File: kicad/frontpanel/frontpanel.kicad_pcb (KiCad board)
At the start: 2 copper layers, 40.6 x 128.5 mm, 21 parts

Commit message: Update frontpanel.
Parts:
- moved REF** 0.64 mm to (120.4, 39.5)
- moved REF** 0.64 mm to (120.4, 56.3)
- moved REF** 0.63 mm to (133.1, 39.5)
- moved REF** 0.63 mm to (145.8, 56.3)
- moved REF** 0.63 mm to (133.1, 56.3)
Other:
- board text added: "ACT"
- board text added: "ARP LEN"
- board text added: "CC1"
- board text added: "CC2"
- board text added: "CV1"
- board text added: "CV2"
- board text added: "GATE1"
- board text added: "GATE2"
- board text added: "JLCJLCJLCJLC"
- board text added: "MIDI IN"
- board text added: "Miarph"
- board text added: "P1"
- board text added: "P2"
- board text added: "P3"
- board text added: "P4"
- board text added: "P5"
- board text added: "P6"
- board text added: "P7"
- board text added: "P8"
- board text added: "TOMARUS"
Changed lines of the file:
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@@
   (general
     (thickness 1.6)
-    (drawings 16)
+    (drawings 34)
     (tracks 0)
     (zones 0)
@@
     (32 B.Adhes user hide)
     (33 F.Adhes user hide)
-    (34 B.Paste user hide)
-    (35 F.Paste user hide)
+    (34 B.Paste user)
+    (35 F.Paste user)
     (36 B.SilkS user)
     (37 F.SilkS user)
@@
     (39 F.Mask user hide)
     (40 Dwgs.User user hide)
-    (41 Cmts.User user)
+    (41 Cmts.User user hide)
     (42 Eco1.User user)
     (43 Eco2.User user hide)
@@
   )
   (module MountingHole:MountingHole_6.4mm_M6 (layer F.Cu)
-    (at 132.461 39.497)
+    (at 133.096 39.497)
     (descr "Mounting Hole 6.4mm, no annular, M6")
     (tags "mounting hole 6.4mm no annular m6")
@@
   )
   (module MountingHole:MountingHole_3.2mm_M3 (layer F.Cu)
-    (at 119.761 39.497)
+    (at 120.396 39.497)
     (descr "Mounting Hole 3.2mm, no annular, M3")
     (tags "mounting hole 3.2mm no annular m3")
@@
   )
   (module MountingHole:MountingHole_6.4mm_M6_Pad (layer F.Cu)
-    (at 119.761 56.261)
-    (descr "Mounting Hole 6.4mm, M6")
-    (tags "mounting hole 6.4mm m6")
-    (attr virtual)
-    (fp_text reference REF** (at 0 -7.4) (layer F.SilkS) hide
-      (effects (font (size 1 1) (thickness 0.15)))
-    )
-    (fp_text value MountingHole_6.4mm_M6_Pad (at 0 7.4) (layer F.Fab)
-      (effects (font (size 1 1) (thickness 0.15)))
-    )
-    (fp_circle (center 0 0) (end 6.65 0) (layer F.CrtYd) (width 0.05))
-    (fp_circle (center 0 0) (end 6.4 0) (layer Cmts.User) (width 0.15))
-    (fp_text user %R (at 0.3 0) (layer F.Fab)
-      (effects (font (size 1 1) (thickness 0.15)))
-    )
-    (pad 1 thru_hole circle (at 0 0) (size 8.4 8.4) (drill 6.4) (layers *.Cu *.Mask))
-  )
-  (module MountingHole:MountingHole_6.4mm_M6_Pad (layer F.Cu)
-    (at 145.161 56.261)
-    (descr "Mounting Hole 6.4mm, M6")
-    (tags "mounting hole 6.4mm m6")
-    (attr virtual)
-    (fp_text reference REF** (at 0 -7.4) (layer F.SilkS) hide
-      (effects (font (size 1 1) (thickness 0.15)))
-    )
-    (fp_text value MountingHole_6.4mm_M6_Pad (at 0 7.4) (layer F.Fab)
-      (effects (font (size 1 1) (thickness 0.15)))
-    )
-    (fp_circle (center 0 0) (end 6.65 0) (layer F.CrtYd) (width 0.05))
-    (fp_circle (center 0 0) (end 6.4 0) (layer Cmts.User) (width 0.15))
-    (fp_text user %R (at 0.3 0) (layer F.Fab)
-      (effects (font (size 1 1) (thickness 0.15)))
-    )
-    (pad 1 thru_hole circle (at 0 0) (size 8.4 8.4) (drill 6.4) (layers *.Cu *.Mask))
-  )
-  (module MountingHole:MountingHole_6.4mm_M6_Pad (layer F.Cu)
-    (at 132.461 56.261)
+    (at 120.396 56.261)
+    (descr "Mounting Hole 6.4mm, M6")
+    (tags "mounting hole 6.4mm m6")
+    (attr virtual)
+    (fp_text reference REF** (at 0 -7.4) (layer F.SilkS) hide
+      (effects (font (size 1 1) (thickness 0.15)))
+    )
+    (fp_text value MountingHole_6.4mm_M6_Pad (at 0 7.4) (layer F.Fab)
+      (effects (font (size 1 1) (thickness 0.15)))
+    )
+    (fp_circle (center 0 0) (end 6.65 0) (layer F.CrtYd) (width 0.05))
+    (fp_circle (center 0 0) (end 6.4 0) (layer Cmts.User) (width 0.15))
+    (fp_text user %R (at 0.3 0) (layer F.Fab)
+      (effects (font (size 1 1) (thickness 0.15)))
+    )
+    (pad 1 thru_hole circle (at 0 0) (size 8.4 8.4) (drill 6.4) (layers *.Cu *.Mask))
+  )
+  (module MountingHole:MountingHole_6.4mm_M6_Pad (layer F.Cu)
+    (at 145.796 56.261)
+    (descr "Mounting Hole 6.4mm, M6")
+    (tags "mounting hole 6.4mm m6")
+    (attr virtual)
+    (fp_text reference REF** (at 0 -7.4) (layer F.SilkS) hide
+      (effects (font (size 1 1) (thickness 0.15)))
+    )
+    (fp_text value MountingHole_6.4mm_M6_Pad (at 0 7.4) (layer F.Fab)
+      (effects (font (size 1 1) (thickness 0.15)))
+    )
+    (fp_circle (center 0 0) (end 6.65 0) (layer F.CrtYd) (width 0.05))
+    (fp_circle (center 0 0) (end 6.4 0) (layer Cmts.User) (width 0.15))
+    (fp_text user %R (at 0.3 0) (layer F.Fab)
+      (effects (font (size 1 1) (thickness 0.15)))
+    )
+    (pad 1 thru_hole circle (at 0 0) (size 8.4 8.4) (drill 6.4) (layers *.Cu *.Mask))
+  )
+  (module MountingHole:MountingHole_6.4mm_M6_Pad (layer F.Cu)
+    (at 133.096 56.261)
     (descr "Mounting Hole 6.4mm, M6")
     (tags "mounting hole 6.4mm m6")
@@
     )
     (pad 1 thru_hole circle (at 0 0) (size 8.4 8.4) (drill 6.4) (layers *.Cu *.Mask))
+  )
+  (gr_text JLCJLCJLCJLC (at 133.096 132.08) (layer F.SilkS)
+    (effects (font (size 1.5 1.5) (thickness 0.3)))
+  )
+  (gr_text ACT (at 120.396 43.18) (layer B.SilkS)
+    (effects (font (size 1 1) (thickness 0.25)) (justify mirror))
+  )
+  (gr_text "ARP LEN" (at 133.096 45.72) (layer B.SilkS)
+    (effects (font (size 1.5 1.5) (thickness 0.3)) (justify mirror))
+  )
+  (gr_text TOMARUS (at 132.842 140.081) (layer B.SilkS)
+    (effects (font (size 2.5 2.5) (thickness 0.5)) (justify mirror))
+  )
+  (gr_text Miarph (at 132.842 17.526) (layer B.SilkS)
+    (effects (font (size 3 3) (thickness 0.5)) (justify mirror))
+  )
+  (gr_text GATE2 (at 120.396 109.22) (layer B.SilkS)
+    (effects (font (size 1.5 1.5) (thickness 0.3)) (justify mirror))
+  )
+  (gr_text CV2 (at 120.396 93.98) (layer B.SilkS)
+    (effects (font (size 1.5 1.5) (thickness 0.3)) (justify mirror))
+  )
+  (gr_text GATE1 (at 120.396 78.74) (layer B.SilkS)
+    (effects (font (size 1.5 1.5) (thickness 0.3)) (justify mirror))
+  )
+  (gr_text CV1 (at 120.396 63.5) (layer B.SilkS)
+    (effects (font (size 1.5 1.5) (thickness 0.3)) (justify mirror))
+  )
+  (gr_text P6 (at 133.096 93.98) (layer B.SilkS)
+    (effects (font (size 1.5 1.5) (thickness 0.3)) (justify mirror))
+  )
+  (gr_text P5 (at 145.796 93.98) (layer B.SilkS)
+    (effects (font (size 1.5 1.5) (thickness 0.3)) (justify mirror))
+  )
+  (gr_text P4 (at 133.096 78.74) (layer B.SilkS)
+    (effects (font (size 1.5 1.5) (thickness 0.3)) (justify mirror))
+  )
+  (gr_text P3 (at 145.796 78.74) (layer B.SilkS)
+    (effects (font (size 1.5 1.5) (thickness 0.3)) (justify mirror))
+  )
+  (gr_text P2 (at 133.096 63.5) (layer B.SilkS)
+    (effects (font (size 1.5 1.5) (thickness 0.3)) (justify mirror))
+  )
+  (gr_text P1 (at 145.796 63.5) (layer B.SilkS)
+    (effects (font (size 1.5 1.5) (thickness 0.3)) (justify mirror))
+  )
+  (gr_text P8 (at 133.096 109.22) (layer B.SilkS)
+    (effects (font (size 1.5 1.5) (thickness 0.3)) (justify mirror))
+  )
+  (gr_text P7 (at 145.796 109.22) (layer B.SilkS)
+    (effects (font (size 1.5 1.5) (thickness 0.3)) (justify mirror))
+  )
+  (gr_text CC2 (at 120.396 124.46) (layer B.SilkS)
+    (effects (font (size 1.5 1.5) (thickness 0.3)) (justify mirror))
+  )
+  (gr_text CC1 (at 133.096 124.46) (layer B.SilkS)
+    (effects (font (size 1.5 1.5) (thickness 0.3)) (justify mirror))
+  )
+  (gr_text "MIDI IN" (at 145.796 124.46) (layer B.SilkS)
+    (effects (font (size 1.5 1.5) (thickness 0.3)) (justify mirror))
   )
   (dimension 40.607945 (width 0.3) (layer F.SilkS)
@@
   (gr_line (start 153.416 14.478) (end 153.416 14.732) (layer Edge.Cuts) (width 0.15))
   (dimension 128.491945 (width 0.3) (layer F.SilkS)
-    (gr_text "128.492 mm" (at 158.269779 78.755981 270.0006131) (layer F.SilkS)
+    (gr_text "128.492 mm" (at 158.904779 78.755981 270.0006131) (layer F.SilkS)
       (effects (font (size 1.5 1.5) (thickness 0.3)))
     )
-    (feature1 (pts (xy 153.884467 143.002) (xy 156.756888 143.001969)))
-    (feature2 (pts (xy 153.883092 14.510055) (xy 156.755513 14.510024)))
-    (crossbar (pts (xy 156.169092 14.510031) (xy 156.170467 143.001976)))
-    (arrow1a (pts (xy 156.170467 143.001976) (xy 155.584034 141.875479)))
-    (arrow1b (pts (xy 156.170467 143.001976) (xy 156.756876 141.875466)))
-    (arrow2a (pts (xy 156.169092 14.510031) (xy 155.582683 15.636541)))
-    (arrow2b (pts (xy 156.169092 14.510031) (xy 156.755525 15.636528)))
+    (feature1 (pts (xy 154.519467 143.002) (xy 157.391888 143.001969)))
+    (feature2 (pts (xy 154.518092 14.510055) (xy 157.390513 14.510024)))
+    (crossbar (pts (xy 156.804092 14.510031) (xy 156.805467 143.001976)))
+    (arrow1a (pts (xy 156.805467 143.001976) (xy 156.219034 141.875479)))
+    (arrow1b (pts (xy 156.805467 143.001976) (xy 157.391876 141.875466)))
+    (arrow2a (pts (xy 156.804092 14.510031) (xy 156.217683 15.636541)))
+    (arrow2b (pts (xy 156.804092 14.510031) (xy 157.390525 15.636528)))
   )
   (gr_line (start 153.416 142.748) (end 153.416 127) (layer Edge.Cuts) (width 0.15))
@@
   (gr_line (start 112.776 30.48) (end 112.776 14.732) (layer Edge.Cuts) (width 0.15))
   (gr_line (start 112.776 127) (end 112.776 30.48) (layer Edge.Cuts) (width 0.15))
-  (gr_line (start 153.416 127) (end 112.776 127) (layer Edge.Cuts) (width 0.15))
   (gr_line (start 153.416 30.48) (end 153.416 127) (layer Edge.Cuts) (width 0.15))
-  (gr_line (start 112.776 30.48) (end 153.416 30.48) (layer Edge.Cuts) (width 0.15))
 )

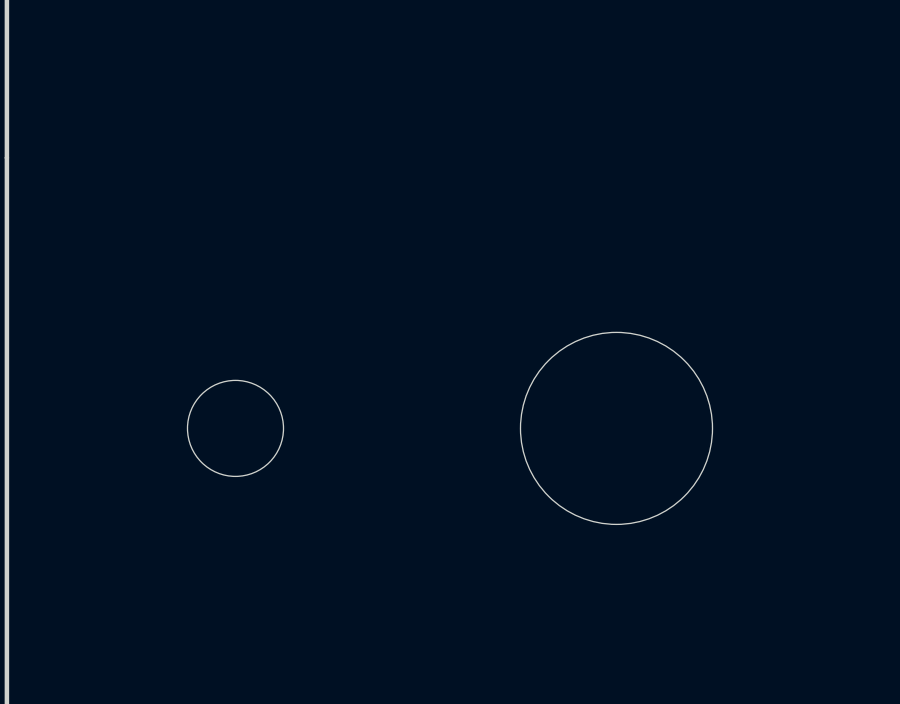
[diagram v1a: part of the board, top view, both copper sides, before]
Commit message: Update some symbols + footprints.
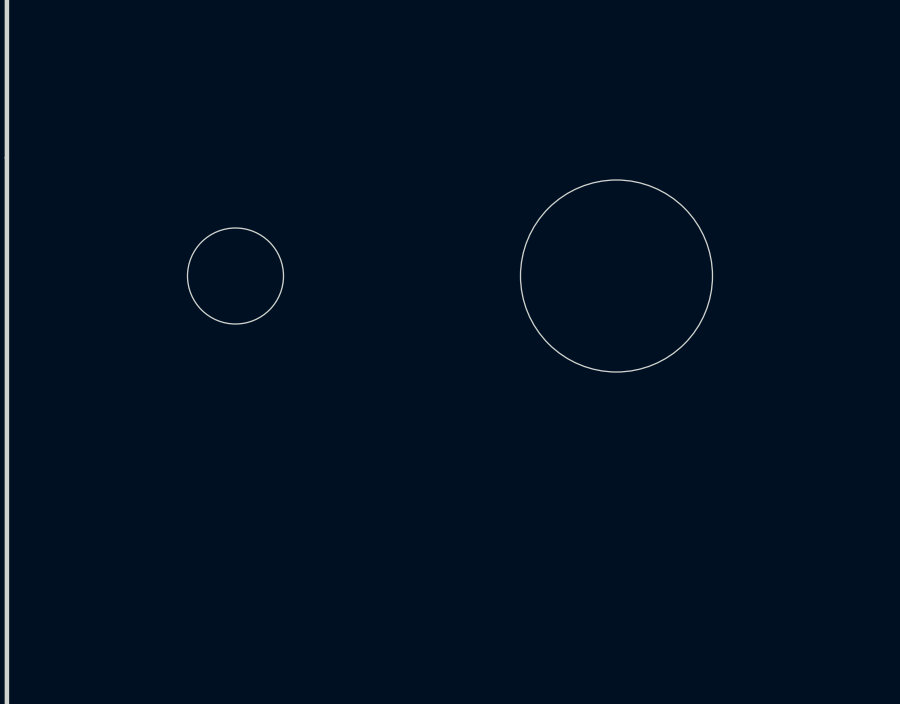
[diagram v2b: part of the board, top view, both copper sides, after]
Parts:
- moved REF** 5.08 mm to (133.1, 34.4)
- moved REF** 5.08 mm to (120.4, 34.4)
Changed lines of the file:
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@@
   (general
     (thickness 1.6)
-    (drawings 34)
+    (drawings 35)
     (tracks 0)
     (zones 0)
@@
       (outputformat 1)
       (mirror false)
-      (drillshape 1)
+      (drillshape 0)
       (scaleselection 1)
       (outputdirectory ""))
@@
   )
   (module MountingHole:MountingHole_6.4mm_M6 (layer F.Cu)
-    (at 133.096 39.497)
+    (at 133.096 34.417)
     (descr "Mounting Hole 6.4mm, no annular, M6")
     (tags "mounting hole 6.4mm no annular m6")
@@
   )
   (module MountingHole:MountingHole_3.2mm_M3 (layer F.Cu)
-    (at 120.396 39.497)
+    (at 120.396 34.417)
     (descr "Mounting Hole 3.2mm, no annular, M3")
     (tags "mounting hole 3.2mm no annular m3")
@@
     (pad 1 thru_hole circle (at 0 0) (size 8.4 8.4) (drill 6.4) (layers *.Cu *.Mask))
   )
+  (gr_poly (pts (xy 141.732 122.936) (xy 139.7 122.936) (xy 139.7 111.76) (xy 152.4 111.76) (xy 152.4 122.936)) (layer B.SilkS) (width 0.15))
   (gr_text JLCJLCJLCJLC (at 133.096 132.08) (layer F.SilkS)
     (effects (font (size 1.5 1.5) (thickness 0.3)))
   )
-  (gr_text ACT (at 120.396 43.18) (layer B.SilkS)
+  (gr_text ACT (at 120.396 38.1) (layer B.SilkS)
     (effects (font (size 1 1) (thickness 0.25)) (justify mirror))
   )
-  (gr_text "ARP LEN" (at 133.096 45.72) (layer B.SilkS)
+  (gr_text "ARP LEN" (at 133.096 40.64) (layer B.SilkS)
     (effects (font (size 1.5 1.5) (thickness 0.3)) (justify mirror))
   )

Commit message: Small production updates.
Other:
- rule pad_to_mask_clearance: 0.051 -> 0
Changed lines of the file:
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@@
   (general
     (thickness 1.6)
-    (drawings 35)
+    (drawings 33)
     (tracks 0)
     (zones 0)
@@
     (36 B.SilkS user)
     (37 F.SilkS user)
-    (38 B.Mask user hide)
+    (38 B.Mask user)
     (39 F.Mask user hide)
     (40 Dwgs.User user hide)
@@
     (pad_size 8.4 8.4)
     (pad_drill 6.4)
-    (pad_to_mask_clearance 0.051)
+    (pad_to_mask_clearance 0)
     (solder_mask_min_width 0.25)
     (aux_axis_origin 112.776 14.478)
     (visible_elements FFFFFF7F)
     (pcbplotparams
-      (layerselection 0x010fc_ffffffff)
+      (layerselection 0x010f0_ffffffff)
       (usegerberextensions false)
       (usegerberattributes false)
@@
       (psa4output false)
       (plotreference true)
-      (plotvalue true)
+      (plotvalue false)
       (plotinvisibletext false)
       (padsonsilk false)
@@
       (drillshape 0)
       (scaleselection 1)
-      (outputdirectory ""))
+      (outputdirectory "plots/"))
   )
   (net 0 "")
@@
     (effects (font (size 1.5 1.5) (thickness 0.3)) (justify mirror))
   )
-  (dimension 40.607945 (width 0.3) (layer F.SilkS)
-    (gr_text "40.608 mm" (at 133.112131 146.708222 0.001940056233) (layer F.SilkS)
-      (effects (font (size 1.5 1.5) (thickness 0.3)))
-    )
-    (feature1 (pts (xy 153.416 143.619796) (xy 153.416053 145.193956)))
-    (feature2 (pts (xy 112.808055 143.621171) (xy 112.808108 145.195331)))
-    (crossbar (pts (xy 112.808088 144.60891) (xy 153.416033 144.607535)))
-    (arrow1a (pts (xy 153.416033 144.607535) (xy 152.289549 145.193994)))
-    (arrow1b (pts (xy 153.416033 144.607535) (xy 152.289509 144.021152)))
-    (arrow2a (pts (xy 112.808088 144.60891) (xy 113.934612 145.195293)))
-    (arrow2b (pts (xy 112.808088 144.60891) (xy 113.934572 144.022451)))
-  )
   (gr_line (start 153.416 143.002) (end 153.416 142.748) (layer Edge.Cuts) (width 0.15))
   (gr_line (start 112.776 143.002) (end 112.776 142.748) (layer Edge.Cuts) (width 0.15))
   (gr_line (start 112.776 14.478) (end 112.776 14.732) (layer Edge.Cuts) (width 0.15))
   (gr_line (start 153.416 14.478) (end 153.416 14.732) (layer Edge.Cuts) (width 0.15))
-  (dimension 128.491945 (width 0.3) (layer F.SilkS)
-    (gr_text "128.492 mm" (at 158.904779 78.755981 270.0006131) (layer F.SilkS)
-      (effects (font (size 1.5 1.5) (thickness 0.3)))
-    )
-    (feature1 (pts (xy 154.519467 143.002) (xy 157.391888 143.001969)))
-    (feature2 (pts (xy 154.518092 14.510055) (xy 157.390513 14.510024)))
-    (crossbar (pts (xy 156.804092 14.510031) (xy 156.805467 143.001976)))
-    (arrow1a (pts (xy 156.805467 143.001976) (xy 156.219034 141.875479)))
-    (arrow1b (pts (xy 156.805467 143.001976) (xy 157.391876 141.875466)))
-    (arrow2a (pts (xy 156.804092 14.510031) (xy 156.217683 15.636541)))
-    (arrow2b (pts (xy 156.804092 14.510031) (xy 157.390525 15.636528)))
-  )
   (gr_line (start 153.416 142.748) (end 153.416 127) (layer Edge.Cuts) (width 0.15))
   (gr_line (start 112.776 143.002) (end 153.416 143.002) (layer Edge.Cuts) (width 0.15))
